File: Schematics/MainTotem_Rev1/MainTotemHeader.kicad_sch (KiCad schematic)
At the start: 0 parts

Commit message: Added RS485 functionality to MainTotemLite
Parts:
- added J4: Conn_02x05_Odd_Even, symbol Connector_Generic:Conn_02x05_Odd_Even
- added SW1: 3-1825010-8, SW6_3-1825010-8_TEC, symbol 6PDTSwitch:3-1825010-8
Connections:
- new net: J4.7 (Pin_7), SW1.1
- new net: J4.4 (Pin_4), SW1.12
- new net: J4.8 (Pin_8), SW1.15
- new net: J4.10 (Pin_10), SW1.18
- new net: J4.3 (Pin_3), SW1.4
- new net: J4.2 (Pin_2), SW1.7
- new net +3V3: J4.1 (Pin_1)
- new net BUSH7BOOT0: SW1.16
- new net BUSH7NRST: SW1.6
- new net BUSH7SWCLK: SW1.10
- new net BUSH7SWDIO: SW1.9
- new net BUSH7UARTRX: SW1.13
- new net BUSHH7UARTTX: SW1.3
- new net GND: J4.5 (Pin_5), J4.9 (Pin_9)
- new net H7BOOT0: SW1.17
- new net H7NRST: SW1.5
- new net H7SWCLK: SW1.11
- new net H7SWDIO: SW1.8
- new net H7SWO: J4.6 (Pin_6)
- new net H7UARTRX: SW1.14
- new net H7UARTTX: SW1.2
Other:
- note added: "Got the Switch Pinout from a random site online, could be wrong. Check with multimeter the connections"

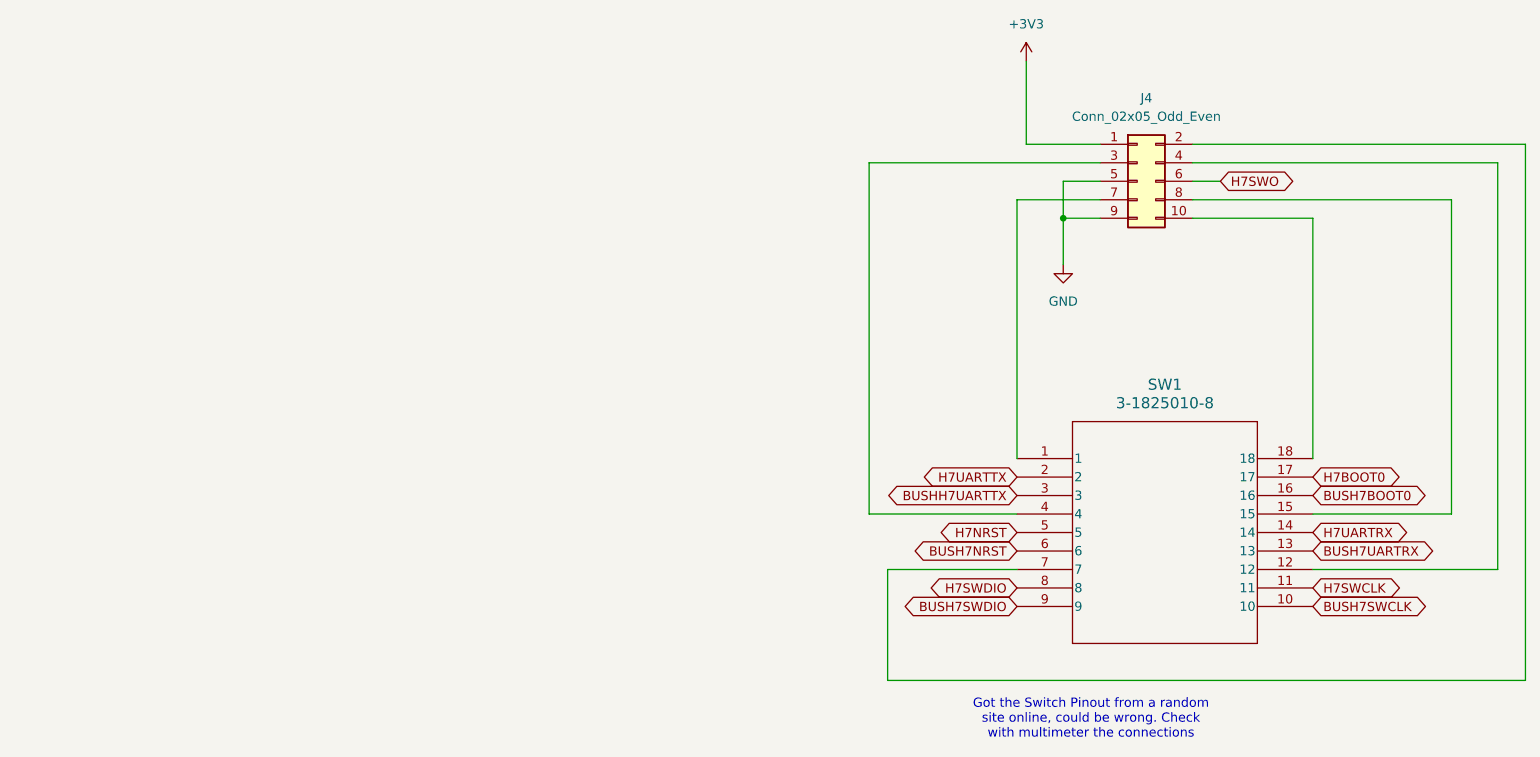
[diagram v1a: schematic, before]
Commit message: Layout Edits for Mezzanine Connector routing
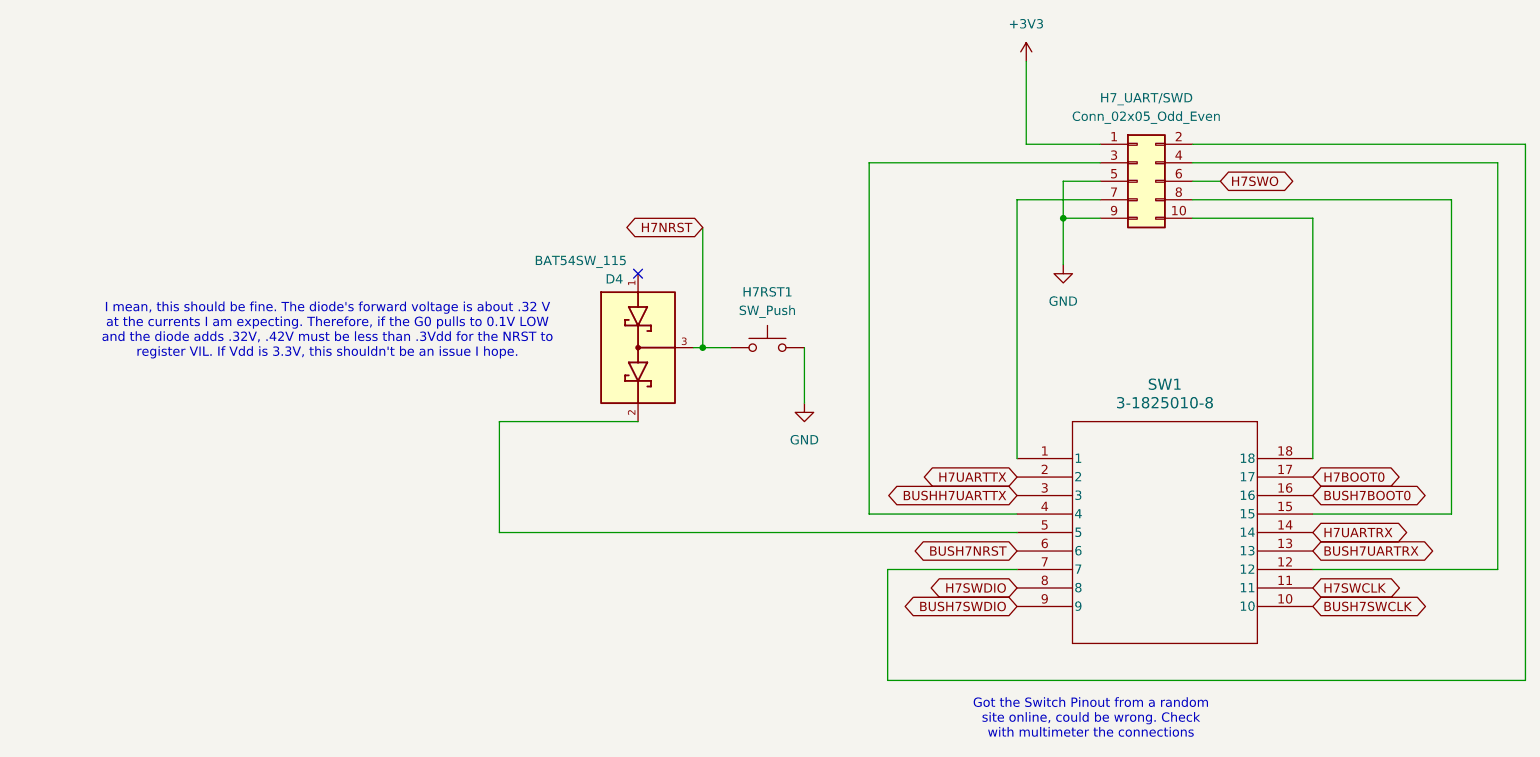
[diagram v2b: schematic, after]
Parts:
- added D4: BAT54SW_115, BAT54SW_115:BAT54SW_115, symbol BAT54SW_115:BAT54SW_115
- added H7RST1: SW_Push, Button_Switch_SMD:SW_SPST_PTS645Sx43SMTR92, symbol Switch:SW_Push
- H7_UART/SWD: renamed from J4; footprint (none) -> Connector_PinHeader_2.54mm:PinHeader_2x05_P2.54mm_Vertical
- SW1: footprint SW6_3-1825010-8_TEC -> 6PDTSwitch:SW6_3-1825010-8_TEC
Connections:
- net GND: now also H7RST1.2
- net H7NRST: now also D4.3, H7RST1.1; no longer SW1.5
- new net: D4.2, SW1.5
- no-connect marks 0 -> 1
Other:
- note added: "I mean, this should be fine. The diode's forward voltage is about .32 V at the currents I am expecting. Therefore, if the G0 pulls to 0.1V LOW and the diode adds .32V, .42V must be less than .3Vdd for the NRST to register VIL. If Vdd is 3.3V, this shouldn't be an issue I hope."

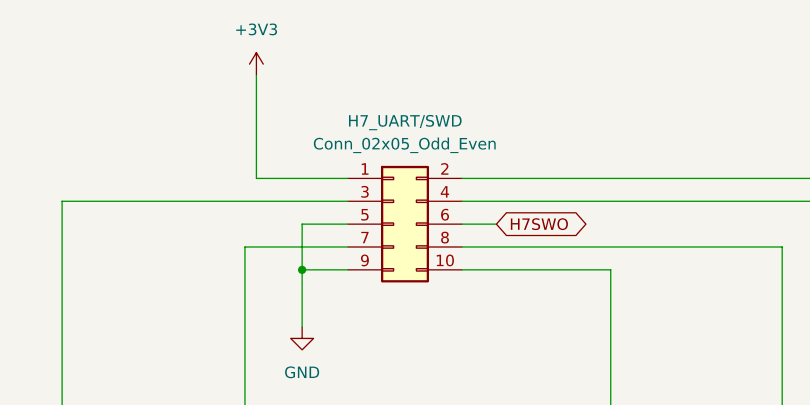
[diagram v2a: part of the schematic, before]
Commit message: Rerouting layout to resolve collision issues
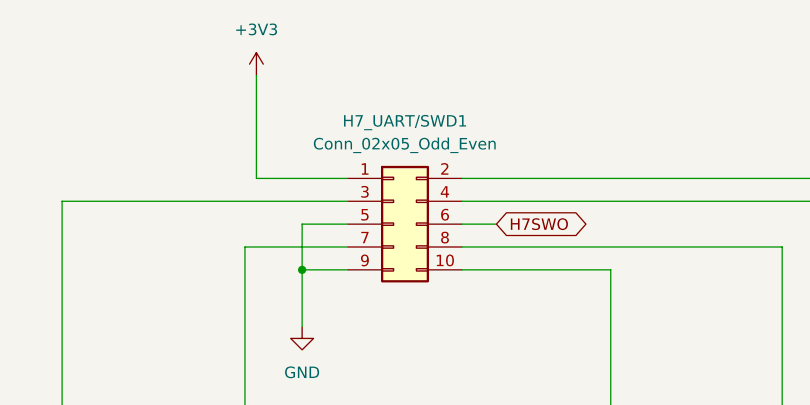
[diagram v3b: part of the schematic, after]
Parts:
- renumbered H7_UART/SWD to H7_UART/SWD1
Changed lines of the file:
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@@
 		(dnp no)
 		(fields_autoplaced yes)
-		(property "Reference" "H7_UART/SWD"
+		(property "Reference" "H7_UART/SWD1"
 			(at 162.56 81.28 0)
 			(effects
@@
 			(project ""
 				(path "/f88ba0f4-041f-4cf3-b904-3ea5c6101abb/1663cdcb-fd8a-4b7c-9fc6-67a30a6bff25"
-					(reference "H7_UART/SWD")
+					(reference "H7_UART/SWD1")
 					(unit 1)
 				)
